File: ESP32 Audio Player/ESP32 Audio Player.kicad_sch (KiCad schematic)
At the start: 8 parts, among them SW1 SW_Push, SW2 SW_Push, SW3 SW_Push, U1 TP4056, U2 OLED

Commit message: Completed main firmware
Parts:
- SD1: footprint Extras:SD Card Reader -> Micro SD Card Reader:MODULE_MICROSD_SPI_OR_SDIO_CARD
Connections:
- net +5V: no longer SD1.2 (VCC)
- net GND: now also SD1.6 (GND); no longer SD1.1 (GND)
- net at MCU1.8 (D5): now also SD1.2 (CS); no longer SD1.6 (CS)
- net 3V3: now reaches MCU1.1 (3V3)
- net 3V3: now also SD1.1 (3V3)
- no-connect marks 23 -> 22
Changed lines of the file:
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@@
-	)
-	(no_connect
-		(at 88.9 43.18)
 	)
 	(no_connect
@@
 		)
 	)
+	(global_label "3V3"
+		(shape input)
+		(at 88.9 43.18 0)
+		(fields_autoplaced yes)
+		(effects
+			(font
+				(size 1.27 1.27)
+			)
+			(justify left)
+		)
+		(property "Intersheetrefs" "${INTERSHEET_REFS}"
+			(at 95.3928 43.18 0)
+			(hide yes)
+			(show_name no)
+			(do_not_autoplace no)
+			(effects
+				(font
+					(size 1.27 1.27)
+				)
+				(justify left)
+			)
+		)
+	)
 	(global_label "5V"
 		(shape input)
@@
 		)
 	)
-	(global_label "5V"
+	(global_label "3V3"
 		(shape input)
 		(at 104.14 95.25 180)
@@
 		)
 		(property "Intersheetrefs" "${INTERSHEET_REFS}"
-			(at 98.8567 95.25 0)
+			(at 97.6472 95.25 0)
 			(hide yes)
 			(show_name no)
@@
 			)
 		)
-		(property "Footprint" "Extras:SD Card Reader"
+		(property "Footprint" "Micro SD Card Reader:MODULE_MICROSD_SPI_OR_SDIO_CARD"
 			(at 106.68 86.36 0)
 			(hide yes)

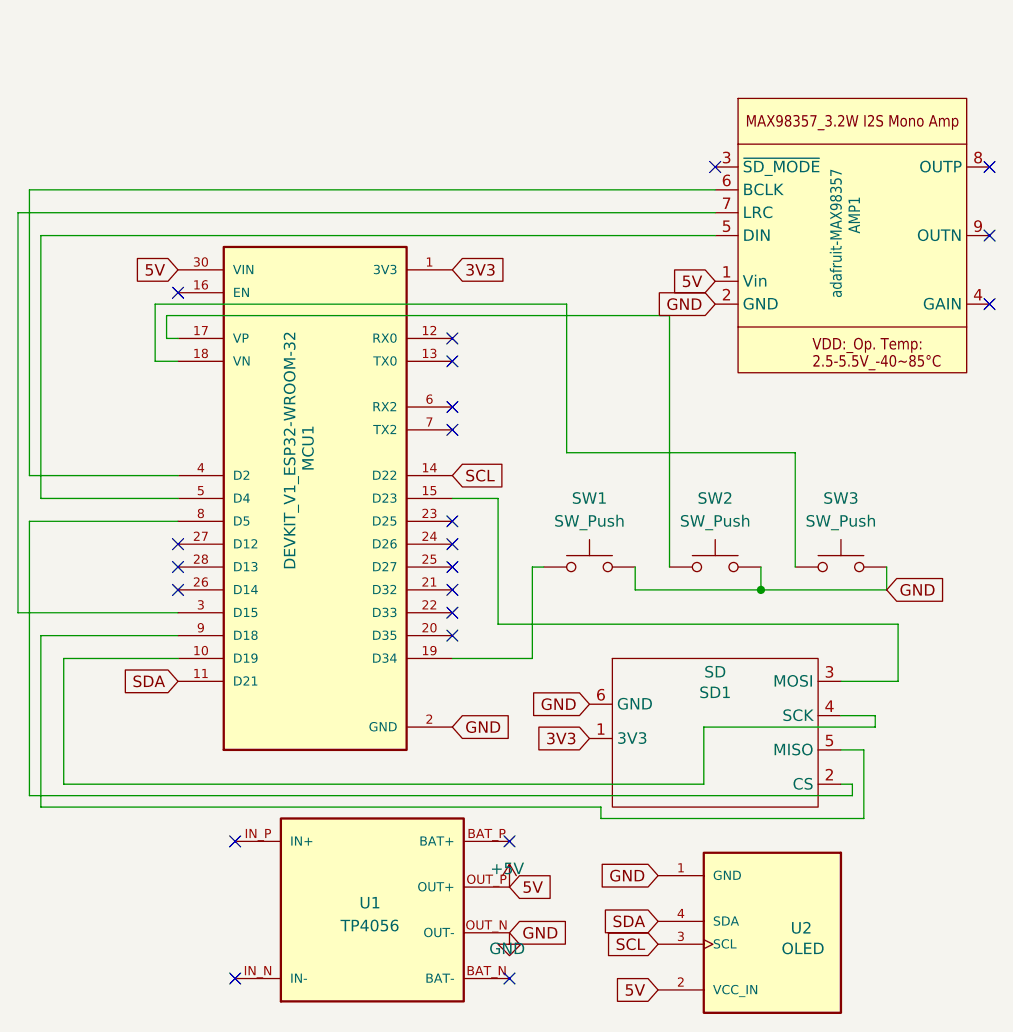
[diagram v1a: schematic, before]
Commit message: Added README and Updated PCB
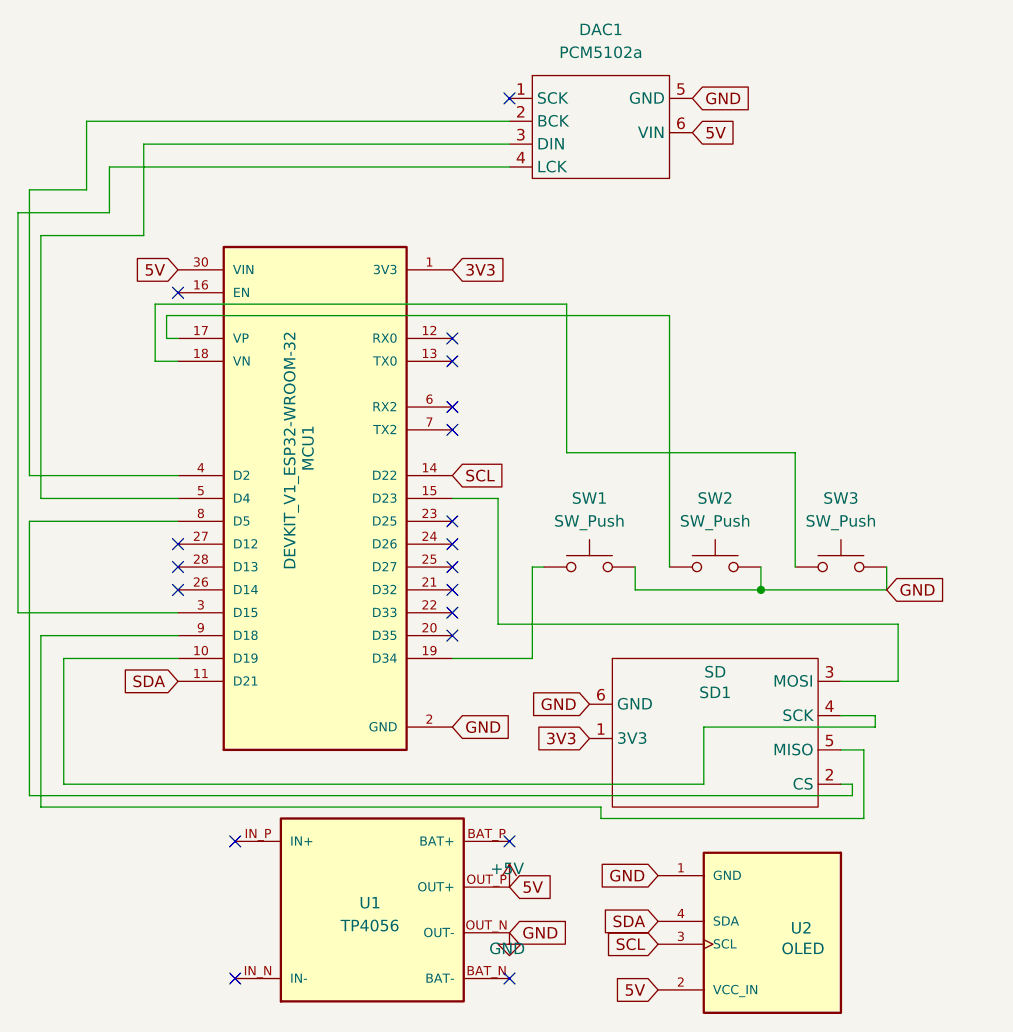
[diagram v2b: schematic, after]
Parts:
- removed AMP1: adafruit-MAX98357, MAX98357A:adafruit-MAX98357, symbol adafruit-MAX98357:adafruit-MAX98357
- added DAC1: PCM5102a, PCM5102a:GY-PCM5102, symbol PCM5102a:PCM5102
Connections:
- net +5V: now also DAC1.6 (VIN)
- net GND: now also DAC1.5 (GND)
- net at MCU1.5 (D4): now also DAC1.3 (DIN)
- net at MCU1.4 (D2): now also DAC1.2 (BCK)
- net at MCU1.3 (D15): now also DAC1.4 (LCK)
- no-connect marks 22 -> 19
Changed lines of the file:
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@@
 	)
 	(no_connect
-		(at 148.59 31.75)
+		(at 95.25 24.13)
 	)
 	(no_connect
@@
 	)
 	(no_connect
-		(at 148.59 46.99)
-	)
-	(no_connect
 		(at 88.9 83.82)
 	)
@@
 	)
 	(no_connect
-		(at 148.59 39.37)
-	)
-	(no_connect
-		(at 118.11 31.75)
-	)
-	(no_connect
 		(at 95.25 121.92)
 	)
@@
 	(wire
 		(pts
+			(xy 48.26 34.29) (xy 41.91 34.29)
+		)
+		(stroke
+			(width 0)
+			(type default)
+		)
+	)
+	(wire
+		(pts
+			(xy 95.25 26.67) (xy 48.26 26.67)
+		)
+		(stroke
+			(width 0)
+			(type default)
+		)
+	)
+	(wire
+		(pts
 			(xy 138.43 88.9) (xy 132.08 88.9)
 		)
@@
 	(wire
 		(pts
+			(xy 95.25 31.75) (xy 50.8 31.75)
+		)
+		(stroke
+			(width 0)
+			(type default)
+		)
+	)
+	(wire
+		(pts
 			(xy 135.89 93.98) (xy 135.89 92.71)
 		)
@@
 	(wire
 		(pts
+			(xy 95.25 29.21) (xy 54.61 29.21)
+		)
+		(stroke
+			(width 0)
+			(type default)
+		)
+	)
+	(wire
+		(pts
 			(xy 101.6 63.5) (xy 127 63.5)
 		)
@@
 	(wire
 		(pts
-			(xy 118.11 36.83) (xy 40.64 36.83)
-		)
-		(stroke
-			(width 0)
-			(type default)
-		)
-	)
-	(wire
-		(pts
 			(xy 97.79 76.2) (xy 97.79 86.36)
 		)
@@
 	(wire
 		(pts
+			(xy 50.8 36.83) (xy 40.64 36.83)
+		)
+		(stroke
+			(width 0)
+			(type default)
+		)
+	)
+	(wire
+		(pts
 			(xy 43.18 68.58) (xy 58.42 68.58)
 		)
@@
 	(wire
 		(pts
+			(xy 48.26 26.67) (xy 48.26 34.29)
+		)
+		(stroke
+			(width 0)
+			(type default)
+		)
+	)
+	(wire
+		(pts
 			(xy 40.64 81.28) (xy 58.42 81.28)
 		)
@@
 	(wire
 		(pts
+			(xy 50.8 31.75) (xy 50.8 36.83)
+		)
+		(stroke
+			(width 0)
+			(type default)
+		)
+	)
+	(wire
+		(pts
 			(xy 134.62 104.14) (xy 134.62 96.52)
 		)
@@
 	(wire
 		(pts
+			(xy 54.61 39.37) (xy 43.18 39.37)
+		)
+		(stroke
+			(width 0)
+			(type default)
+		)
+	)
+	(wire
+		(pts
 			(xy 101.6 46.99) (xy 101.6 63.5)
 		)
@@
 	(wire
 		(pts
-			(xy 118.11 39.37) (xy 43.18 39.37)
-		)
-		(stroke
-			(width 0)
-			(type default)
-		)
-	)
-	(wire
-		(pts
 			(xy 109.22 78.74) (xy 123.19 78.74)
 		)
@@
 	(wire
 		(pts
-			(xy 118.11 34.29) (xy 41.91 34.29)
+			(xy 54.61 29.21) (xy 54.61 39.37)
 		)
 		(stroke
@@
 	(global_label "GND"
 		(shape input)
-		(at 118.11 46.99 180)
+		(at 115.57 24.13 0)
 		(fields_autoplaced yes)
 		(effects
@@
 				(size 1.27 1.27)
 			)
-			(justify right)
+			(justify left)
 		)
 		(property "Intersheetrefs" "${INTERSHEET_REFS}"
-			(at 111.2543 46.99 0)
-			(hide yes)
-			(show_name no)
-			(do_not_autoplace no)
-			(effects
-				(font
-					(size 1.27 1.27)
-				)
-				(justify right)
+			(at 122.4257 24.13 0)
+			(hide yes)
+			(show_name no)
+			(do_not_autoplace no)
+			(effects
+				(font
+					(size 1.27 1.27)
+				)
+				(justify left)
+			)
+		)
+	)
+	(global_label "5V"
+		(shape input)
+		(at 115.57 27.94 0)
+		(fields_autoplaced yes)
+		(effects
+			(font
+				(size 1.27 1.27)
+			)
+			(justify left)
+		)
+		(property "Intersheetrefs" "${INTERSHEET_REFS}"
+			(at 120.8533 27.94 0)
+			(hide yes)
+			(show_name no)
+			(do_not_autoplace no)
+			(effects
+				(font
+					(size 1.27 1.27)
+				)
+				(justify left)
 			)
 		)
@@
 				)
 				(justify left)
-			)
-		)
-	)
-	(global_label "5V"
-		(shape input)
-		(at 118.11 44.45 180)
-		(fields_autoplaced yes)
-		(effects
-			(font
-				(size 1.27 1.27)
-			)
-			(justify right)
-		)
-		(property "Intersheetrefs" "${INTERSHEET_REFS}"
-			(at 112.8267 44.45 0)
-			(hide yes)
-			(show_name no)
-			(do_not_autoplace no)
-			(effects
-				(font
-					(size 1.27 1.27)
-				)
-				(justify right)
 			)
 		)
@@
 				(path "/2332ea6b-93a2-45ca-82a7-c58e44b58b29"
 					(reference "U2")
-					(unit 1)
-				)
-			)
-		)
-	)
-	(symbol
-		(lib_id "adafruit-MAX98357:adafruit-MAX98357")
-		(at 133.35 39.37 0)
-		(unit 1)
-		(body_style 1)
-		(exclude_from_sim no)
-		(in_bom yes)
-		(on_board yes)
-		(in_pos_files yes)
-		(dnp no)
-		(property "Reference" "AMP1"
-			(at 133.604 37.084 90)
-			(show_name no)
-			(do_not_autoplace no)
-			(effects
-				(font
-					(size 1.27 1.0795)
-				)
-			)
-		)
-		(property "Value" "adafruit-MAX98357"
-			(at 131.572 39.116 90)
-			(show_name no)
-			(do_not_autoplace no)
-			(effects
-				(font
-					(size 1.27 1.0795)
-				)
-			)
-		)
-		(property "Footprint" "MAX98357A:adafruit-MAX98357"
-			(at 136.525 59.055 0)
-			(hide yes)
-			(show_name no)
-			(do_not_autoplace no)
-			(effects
-				(font
-					(size 1.27 1.27)
-				)
-			)
-		)
-		(property "Datasheet" ""
-			(at 133.35 39.37 0)
-			(hide yes)
-			(show_name no)
-			(do_not_autoplace no)
-			(effects
-				(font
-					(size 1.27 1.27)
-				)
-			)
-		)
-		(property "Description" ""
-			(at 133.35 39.37 0)
-			(hide yes)
-			(show_name no)
-			(do_not_autoplace no)
-			(effects
-				(font
-					(size 1.27 1.27)
-				)
-			)
-		)
-		(pin "1"
-		)
-		(pin "7"
-		)
-		(pin "5"
-		)
-		(pin "4"
-		)
-		(pin "2"
-		)
-		(pin "8"
-		)
-		(pin "9"
-		)
-		(pin "6"
-		)
-		(pin "3"
-		)
-		(instances
-			(project "ESP32 Audio Player"
-				(path "/2332ea6b-93a2-45ca-82a7-c58e44b58b29"
-					(reference "AMP1")
 					(unit 1)
 				)
@@
 					(unit 1)
 				)
+			)
+		)
+	)
+	(symbol
+		(lib_id "PCM5102a:PCM5102")
+		(at 97.79 21.59 0)
+		(unit 1)
+		(body_style 1)
+		(exclude_from_sim no)
+		(in_bom yes)
+		(on_board yes)
+		(in_pos_files yes)
+		(dnp no)
+		(fields_autoplaced yes)
+		(property "Reference" "DAC1"
+			(at 105.41 16.51 0)
+			(show_name no)
+			(do_not_autoplace no)
+			(effects
+				(font
+					(size 1.27 1.27)
+				)
+			)
+		)
+		(property "Value" "PCM5102a"
+			(at 105.41 19.05 0)
+			(show_name no)
+			(do_not_autoplace no)
+			(effects
+				(font
+					(size 1.27 1.27)
+				)
+			)
+		)
+		(property "Footprint" "PCM5102a:GY-PCM5102"
+			(at 106.426 20.066 0)
+			(hide yes)
+			(show_name no)
+			(do_not_autoplace no)
+			(effects
+				(font
+					(size 1.27 1.27)
+				)
+			)
+		)
+		(property "Datasheet" ""
+			(at 97.79 21.59 0)
+			(hide yes)
+			(show_name no)
+			(do_not_autoplace no)
+			(effects
+				(font
+					(size 1.27 1.27)
+				)
+			)
+		)
+		(property "Description" ""
+			(at 97.79 21.59 0)
+			(hide yes)
+			(show_name no)
+			(do_not_autoplace no)
+			(effects
+				(font
+					(size 1.27 1.27)
+				)
+			)
+		)
+		(pin "1"
+		)
+		(pin "4"
+		)
+		(pin "5"
+		)
+		(pin "3"
+		)
+		(pin "2"
+		)
+		(pin "6"
+		)
+		(instances
+			(project "ESP32 Audio Player"
+				(path "/2332ea6b-93a2-45ca-82a7-c58e44b58b29"
+					(reference "DAC1")
+					(unit 1)
+				)
